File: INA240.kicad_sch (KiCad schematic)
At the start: 0 parts

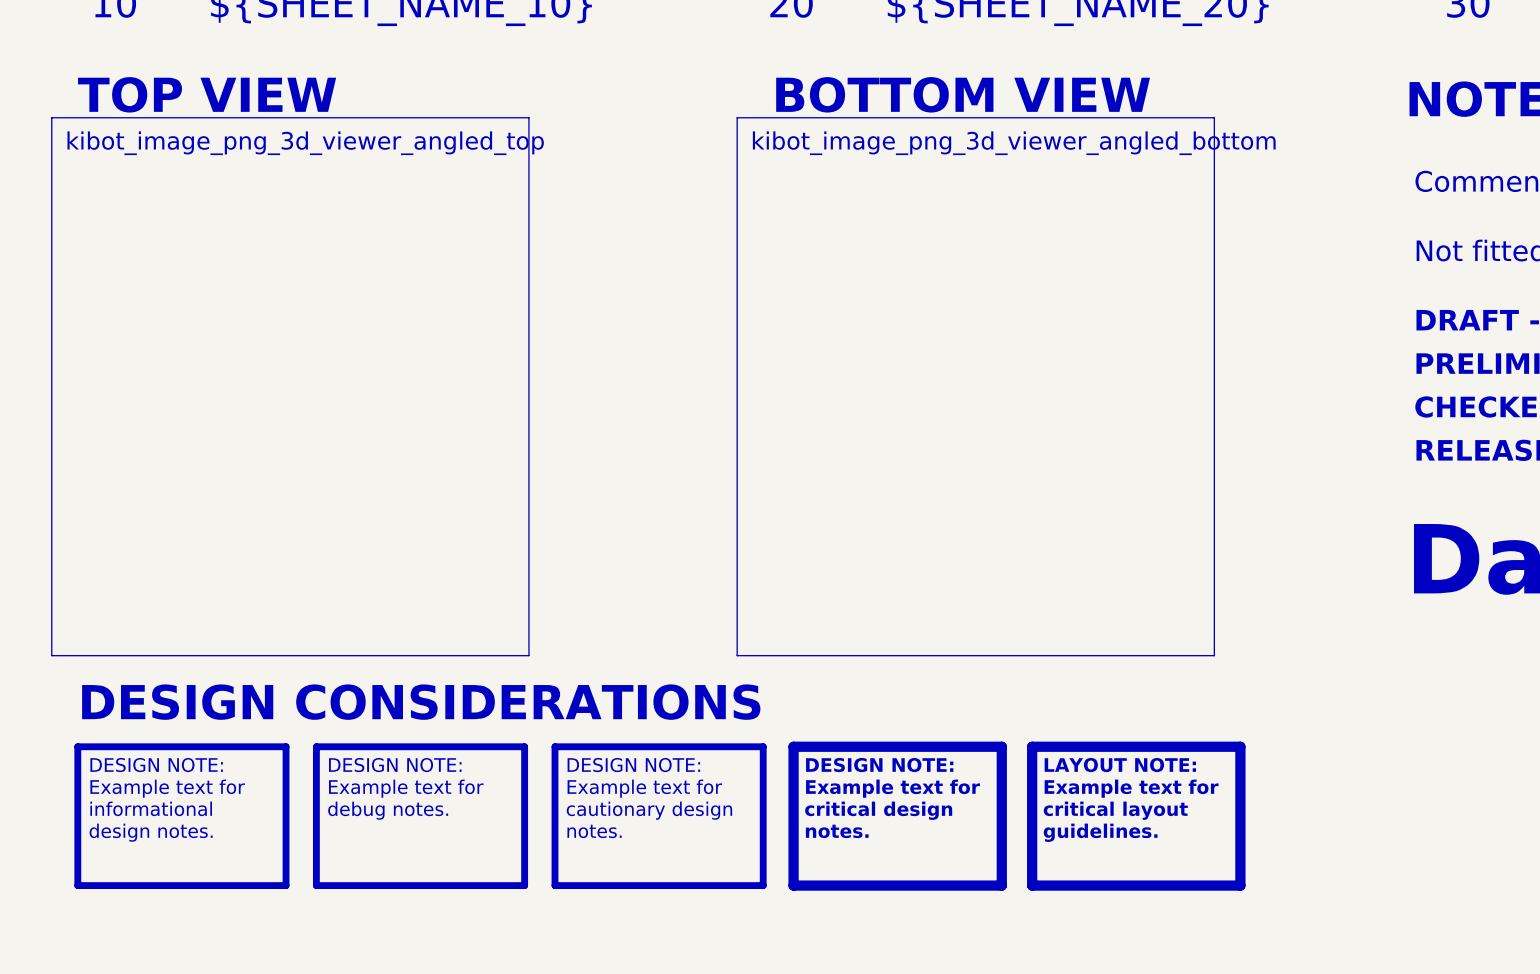
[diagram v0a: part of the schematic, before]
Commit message: Save KiCad 10 design work
Snapshot of the schematic and PCB work done since the initial template
commit: AD7606C-18 ADC, 3x INA241A2 + PBV 1 mOhm shunts, MR60PW phase
connectors, LT8362 boost and LT3045-1 / LTC6655 analog supplies, project
libraries (lib/) and their sym/fp-lib-table.

.gitignore now excludes local history, SpinRender working files, the
stray .step export and Component Search Engine download leftovers.

Co-Authored-By: Claude Opus 5.5 <noreply@anthropic.com>
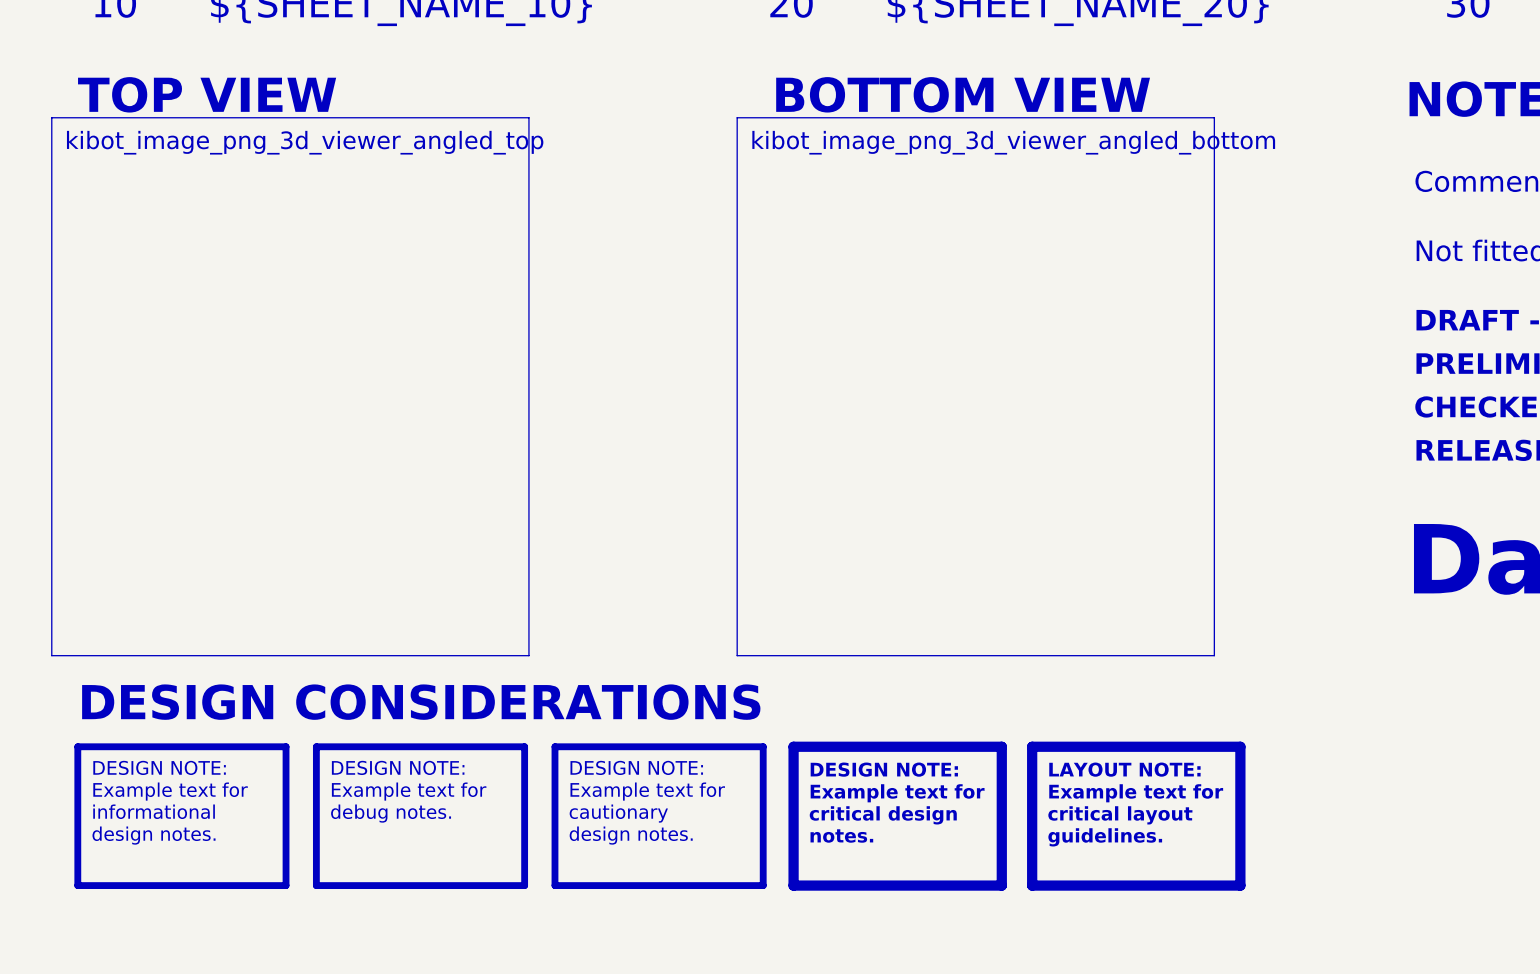
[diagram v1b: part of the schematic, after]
